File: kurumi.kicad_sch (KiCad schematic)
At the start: 20 parts, among them J1 Power input, J2 LEDs, J3 Ext MOSFET/relay, U1 ESP32-C3_SUPERMINI, U2 SN74LVC1T45DRL, U3 TPS54308

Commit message: Parts updates, BOM and CPL
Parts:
- C5: footprint Capacitor_SMD:C_0603_1608Metric_Pad1.08x0.95mm_HandSolder -> Capacitor_SMD:C_0805_2012Metric_Pad1.18x1.45mm_HandSolder
- C6: footprint Capacitor_SMD:CP_Elec_8x10 -> Capacitor_SMD:CP_Elec_8x10.5
- J1, J2, J3, JP1, JP2: now left out of the parts list
- R4: value 100k -> 100K; footprint Resistor_SMD:R_0603_1608Metric_Pad0.98x0.95mm_HandSolder -> Resistor_SMD:R_0805_2012Metric_Pad1.20x1.40mm_HandSolder
- R5: value 13.7k -> 13.7K; footprint Resistor_SMD:R_0603_1608Metric_Pad0.98x0.95mm_HandSolder -> Resistor_SMD:R_0805_2012Metric_Pad1.20x1.40mm_HandSolder
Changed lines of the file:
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@@
 			)
 		)
-		(property "Value" "100k"
+		(property "Value" "100K"
 			(at 81.28 85.09 0)
 			(effects
@@
 			)
 		)
-		(property "Footprint" "Resistor_SMD:R_0603_1608Metric_Pad0.98x0.95mm_HandSolder"
+		(property "Footprint" "Resistor_SMD:R_0805_2012Metric_Pad1.20x1.40mm_HandSolder"
 			(at 82.042 83.82 90)
 			(effects
@@
 			)
 		)
-		(property "Value" "13.7k"
+		(property "Value" "13.7K"
 			(at 81.28 95.25 0)
 			(effects
@@
 			)
 		)
-		(property "Footprint" "Resistor_SMD:R_0603_1608Metric_Pad0.98x0.95mm_HandSolder"
+		(property "Footprint" "Resistor_SMD:R_0805_2012Metric_Pad1.20x1.40mm_HandSolder"
 			(at 82.042 93.98 90)
 			(effects
@@
 			)
 		)
-		(property "Footprint" "Capacitor_SMD:CP_Elec_8x10"
+		(property "Footprint" "Capacitor_SMD:CP_Elec_8x10.5"
 			(at 155.9052 106.68 0)
 			(effects
@@
 			)
 		)
-		(property "Datasheet" "~"
+		(property "Datasheet" "https://www.lcsc.com/datasheet/lcsc_datasheet_2305121703_Honor-Elec-GVM1V471M0810_C5456767.pdf"
 			(at 154.94 102.87 0)
 			(effects
@@
 		(unit 1)
 		(exclude_from_sim no)
-		(in_bom yes)
+		(in_bom no)
 		(on_board yes)
 		(dnp no)
@@
 		(unit 1)
 		(exclude_from_sim no)
-		(in_bom yes)
+		(in_bom no)
 		(on_board yes)
 		(dnp no)
@@
 			)
 		)
-		(property "Datasheet" "~"
+		(property "Datasheet" "https://www.lcsc.com/datasheet/lcsc_datasheet_2402201427_SHOU-HAN-CYA0630-10UH_C5189958.pdf"
 			(at 77.47 78.74 0)
 			(effects
@@
 		(unit 1)
 		(exclude_from_sim no)
-		(in_bom yes)
+		(in_bom no)
 		(on_board yes)
 		(dnp no)
@@
 		(unit 1)
 		(exclude_from_sim no)
-		(in_bom yes)
+		(in_bom no)
 		(on_board yes)
 		(dnp no)
@@
 			)
 		)
-		(property "Footprint" "Capacitor_SMD:C_0603_1608Metric_Pad1.08x0.95mm_HandSolder"
+		(property "Footprint" "Capacitor_SMD:C_0805_2012Metric_Pad1.18x1.45mm_HandSolder"
 			(at 94.9452 92.71 0)
 			(effects
@@
 		(unit 1)
 		(exclude_from_sim no)
-		(in_bom yes)
-		(on_board yes)
-		(dnp no)
+		(in_bom no)
+		(on_board yes)
+		(dnp no)

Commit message: Minor changes
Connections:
- net GND: no longer U3.5 (EN)
- no-connect marks 11 -> 12
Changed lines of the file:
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@@
 	(paper "A4")
 	(junction
-		(at 41.91 95.25)
-		(diameter 0)
-		(color 0 0 0 0)
-	)
-	(junction
 		(at 63.5 57.15)
 		(diameter 0)
@@
 	)
 	(no_connect
+		(at 31.75 83.82)
+	)
+	(no_connect
 		(at 26.67 46.99)
 	)
@@
 	(wire
 		(pts
-			(xy 41.91 88.9) (xy 41.91 95.25)
-		)
-		(stroke
-			(width 0)
-			(type default)
-		)
-	)
-	(wire
-		(pts
 			(xy 125.73 74.93) (xy 125.73 76.2)
 		)
@@
 	(wire
 		(pts
-			(xy 41.91 95.25) (xy 41.91 99.06)
+			(xy 41.91 88.9) (xy 41.91 99.06)
 		)
 		(stroke
@@
 	(wire
 		(pts
-			(xy 31.75 83.82) (xy 29.21 83.82)
-		)
-		(stroke
-			(width 0)
-			(type default)
-		)
-	)
-	(wire
-		(pts
 			(xy 83.82 88.9) (xy 83.82 90.17)
 		)
@@
 	(wire
 		(pts
-			(xy 29.21 83.82) (xy 29.21 95.25)
-		)
-		(stroke
-			(width 0)
-			(type default)
-		)
-	)
-	(wire
-		(pts
 			(xy 25.4 57.15) (xy 63.5 57.15)
 		)
@@
 		)
 		(stroke
-			(width 0)
-			(type default)
-		)
-	)
-	(wire
-		(pts
-			(xy 29.21 95.25) (xy 41.91 95.25)
-		)
-		(stroke

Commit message: Buck converter fix by @CRImier
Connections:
- net FB: now reaches R4.2, R5.1, U3.4 (FB)
- net SW: now reaches C4.1, L1.1, U3.2 (SW)
- net BOOT: now reaches C4.2, U3.6 (BOOT)
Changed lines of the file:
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@@
+		)
+	)
+	(label "BOOT"
+		(at 53.34 78.74 0)
+		(fields_autoplaced yes)
+		(effects
+			(font
+				(size 1.27 1.27)
+			)
+			(justify left bottom)
+		)
+	)
+	(label "SW"
+		(at 53.34 81.28 0)
+		(fields_autoplaced yes)
+		(effects
+			(font
+				(size 1.27 1.27)
+			)
+			(justify left bottom)
+		)
+	)
+	(label "FB"
+		(at 53.34 83.82 0)
+		(fields_autoplaced yes)
+		(effects
+			(font
+				(size 1.27 1.27)
+			)
+			(justify left bottom)
 		)
 	)

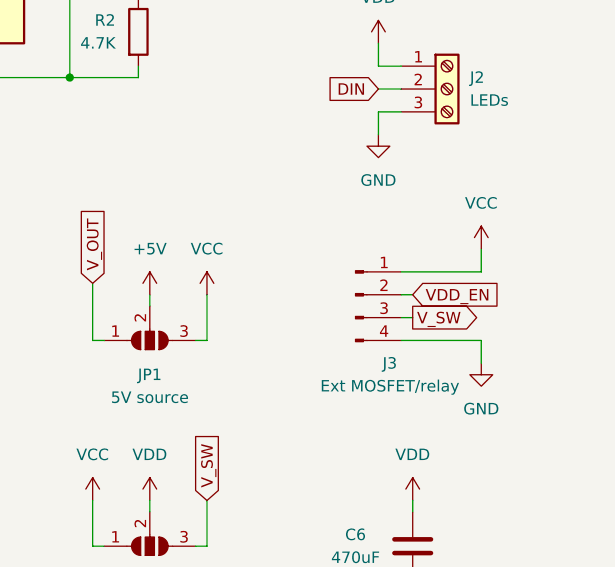
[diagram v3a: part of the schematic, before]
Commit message: Broken out 5V for relays and more
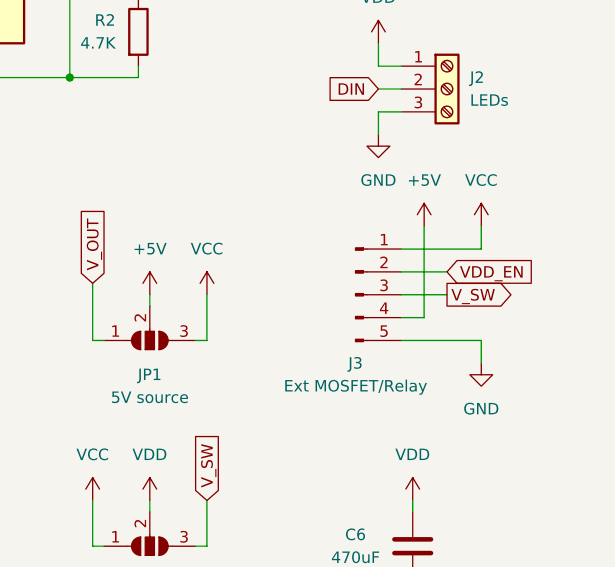
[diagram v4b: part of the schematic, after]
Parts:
- removed J3: Ext MOSFET/relay, Connector_PinHeader_2.54mm:PinHeader_1x04_P2.54mm_Vertical, symbol Connector:Conn_01x04_Pin
- added J3: Ext MOSFET/Relay, Connector_PinHeader_2.54mm:PinHeader_1x05_P2.54mm_Vertical, symbol Connector:Conn_01x05_Pin
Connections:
- net +5V: now also J3.4 (Pin_4)
- net GND: now also J3.5 (Pin_5)
- net VCC: now also J3.1 (Pin_1)
- net VDD_EN: now also J3.2 (Pin_2)
- net V_SW: now also J3.3 (Pin_3)
